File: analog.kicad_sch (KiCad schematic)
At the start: 7 parts, among them J15 Conn_02x12_Odd_Even, J16 Conn_01x06, J17 Conn_01x06, J18 Conn_01x06, J19 Conn_01x06, J20 Conn_01x06, J21 Conn_01x06

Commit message: Finished annotation
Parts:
- renumbered J16 to J1001, J17 to J1002, J18 to J1003, J15 to J1004, J19 to J1005, J20 to J1006, J21 to J1007
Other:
- sheet Analog Input 1 ports: added AIN1, AIN2; removed AOUT1, AOUT2
- sheet Analog Input 2 ports: added AIN1, AIN2; removed AOUT1, AOUT2
- sheet Analog Input 3 ports: added AIN1, AIN2; removed AOUT1, AOUT2
- sheet Analog Input 4 ports: added AIN1, AIN2; removed AOUT1, AOUT2
- sheet Analog Input 5 ports: added AIN1, AIN2; removed AOUT1, AOUT2
- sheet Analog Input 6 ports: added AIN1, AIN2; removed AOUT1, AOUT2
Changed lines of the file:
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@@
   (symbol (lib_id "power:+5V") (at 149.86 186.69 0) (unit 1)
     (in_bom yes) (on_board yes) (dnp no) (fields_autoplaced)
-    (property "Reference" "#PWR0189" (at 149.86 190.5 0)
+    (property "Reference" "#PWR01001" (at 149.86 190.5 0)
       (effects (font (size 1.27 1.27)) hide)
     )
@@
       (project "cad-enc-dec"
         (path "/894df1c3-1a5d-48b0-9966-84d5c2c2c705/27a43937-08d4-4f92-93fe-02e2fba5fc31"
-          (reference "#PWR0189") (unit 1)
+          (reference "#PWR01001") (unit 1)
         )
       )
@@
   (symbol (lib_id "Connector_Generic:Conn_01x06") (at 55.88 213.36 0) (unit 1)
     (in_bom yes) (on_board yes) (dnp no) (fields_autoplaced)
-    (property "Reference" "J19" (at 58.42 213.36 0)
+    (property "Reference" "J1005" (at 58.42 213.36 0)
       (effects (font (size 1.27 1.27)) (justify left))
     )
@@
       (project "cad-enc-dec"
         (path "/894df1c3-1a5d-48b0-9966-84d5c2c2c705/27a43937-08d4-4f92-93fe-02e2fba5fc31"
-          (reference "J19") (unit 1)
+          (reference "J1005") (unit 1)
         )
       )
@@
   (symbol (lib_id "power:+24V") (at 180.34 186.69 0) (unit 1)
     (in_bom yes) (on_board yes) (dnp no) (fields_autoplaced)
-    (property "Reference" "#PWR0190" (at 180.34 190.5 0)
+    (property "Reference" "#PWR01002" (at 180.34 190.5 0)
       (effects (font (size 1.27 1.27)) hide)
     )
@@
       (project "cad-enc-dec"
         (path "/894df1c3-1a5d-48b0-9966-84d5c2c2c705/27a43937-08d4-4f92-93fe-02e2fba5fc31"
-          (reference "#PWR0190") (unit 1)
+          (reference "#PWR01002") (unit 1)
         )
       )
@@
   (symbol (lib_id "Connector_Generic:Conn_01x06") (at 55.88 99.06 0) (unit 1)
     (in_bom yes) (on_board yes) (dnp no) (fields_autoplaced)
-    (property "Reference" "J16" (at 58.42 99.06 0)
+    (property "Reference" "J1001" (at 58.42 99.06 0)
       (effects (font (size 1.27 1.27)) (justify left))
     )
@@
       (project "cad-enc-dec"
         (path "/894df1c3-1a5d-48b0-9966-84d5c2c2c705/27a43937-08d4-4f92-93fe-02e2fba5fc31"
-          (reference "J16") (unit 1)
+          (reference "J1001") (unit 1)
         )
       )
@@
   (symbol (lib_id "power:GND") (at 180.34 214.63 0) (unit 1)
     (in_bom yes) (on_board yes) (dnp no) (fields_autoplaced)
-    (property "Reference" "#PWR0191" (at 180.34 220.98 0)
+    (property "Reference" "#PWR01004" (at 180.34 220.98 0)
       (effects (font (size 1.27 1.27)) hide)
     )
@@
       (project "cad-enc-dec"
         (path "/894df1c3-1a5d-48b0-9966-84d5c2c2c705/27a43937-08d4-4f92-93fe-02e2fba5fc31"
-          (reference "#PWR0191") (unit 1)
+          (reference "#PWR01004") (unit 1)
         )
       )
@@
   (symbol (lib_id "Connector_Generic:Conn_02x12_Odd_Even") (at 163.83 199.39 0) (unit 1)
     (in_bom yes) (on_board yes) (dnp no) (fields_autoplaced)
-    (property "Reference" "J15" (at 165.1 180.34 0)
+    (property "Reference" "J1004" (at 165.1 180.34 0)
       (effects (font (size 1.27 1.27)))
     )
@@
       (project "cad-enc-dec"
         (path "/894df1c3-1a5d-48b0-9966-84d5c2c2c705/27a43937-08d4-4f92-93fe-02e2fba5fc31"
-          (reference "J15") (unit 1)
+          (reference "J1004") (unit 1)
         )
       )
@@
   (symbol (lib_id "Connector_Generic:Conn_01x06") (at 55.88 251.46 0) (unit 1)
     (in_bom yes) (on_board yes) (dnp no) (fields_autoplaced)
-    (property "Reference" "J20" (at 58.42 251.46 0)
+    (property "Reference" "J1006" (at 58.42 251.46 0)
       (effects (font (size 1.27 1.27)) (justify left))
     )
@@
       (project "cad-enc-dec"
         (path "/894df1c3-1a5d-48b0-9966-84d5c2c2c705/27a43937-08d4-4f92-93fe-02e2fba5fc31"
-          (reference "J20") (unit 1)
+          (reference "J1006") (unit 1)
         )
       )
@@
   (symbol (lib_id "power:GND") (at 149.86 214.63 0) (unit 1)
     (in_bom yes) (on_board yes) (dnp no) (fields_autoplaced)
-    (property "Reference" "#PWR0192" (at 149.86 220.98 0)
+    (property "Reference" "#PWR01003" (at 149.86 220.98 0)
       (effects (font (size 1.27 1.27)) hide)
     )
@@
       (project "cad-enc-dec"
         (path "/894df1c3-1a5d-48b0-9966-84d5c2c2c705/27a43937-08d4-4f92-93fe-02e2fba5fc31"
-          (reference "#PWR0192") (unit 1)
+          (reference "#PWR01003") (unit 1)
         )
       )
@@
   (symbol (lib_id "Connector_Generic:Conn_01x06") (at 55.88 175.26 0) (unit 1)
     (in_bom yes) (on_board yes) (dnp no) (fields_autoplaced)
-    (property "Reference" "J18" (at 58.42 175.26 0)
+    (property "Reference" "J1003" (at 58.42 175.26 0)
       (effects (font (size 1.27 1.27)) (justify left))
     )
@@
       (project "cad-enc-dec"
         (path "/894df1c3-1a5d-48b0-9966-84d5c2c2c705/27a43937-08d4-4f92-93fe-02e2fba5fc31"
-          (reference "J18") (unit 1)
+          (reference "J1003") (unit 1)
         )
       )
@@
   (symbol (lib_id "Connector_Generic:Conn_01x06") (at 55.88 137.16 0) (unit 1)
     (in_bom yes) (on_board yes) (dnp no) (fields_autoplaced)
-    (property "Reference" "J17" (at 58.42 137.16 0)
+    (property "Reference" "J1002" (at 58.42 137.16 0)
       (effects (font (size 1.27 1.27)) (justify left))
     )
@@
       (project "cad-enc-dec"
         (path "/894df1c3-1a5d-48b0-9966-84d5c2c2c705/27a43937-08d4-4f92-93fe-02e2fba5fc31"
-          (reference "J17") (unit 1)
+          (reference "J1002") (unit 1)
         )
       )
@@
   (symbol (lib_id "Connector_Generic:Conn_01x06") (at 55.88 289.56 0) (unit 1)
     (in_bom yes) (on_board yes) (dnp no) (fields_autoplaced)
-    (property "Reference" "J21" (at 58.42 289.56 0)
+    (property "Reference" "J1007" (at 58.42 289.56 0)
       (effects (font (size 1.27 1.27)) (justify left))
     )
@@
       (project "cad-enc-dec"
         (path "/894df1c3-1a5d-48b0-9966-84d5c2c2c705/27a43937-08d4-4f92-93fe-02e2fba5fc31"
-          (reference "J21") (unit 1)
+          (reference "J1007") (unit 1)
         )
       )
@@
       (effects (font (size 1.27 1.27)) (justify left top))
     )
-    (pin "AOUT2" output (at 127 107.95 0)
-      (effects (font (size 2.54 2.54)) (justify right))
-    )
-    (pin "AOUT1" output (at 127 102.87 0)
+    (pin "AIN2" output (at 127 107.95 0)
+      (effects (font (size 2.54 2.54)) (justify right))
+    )
+    (pin "AIN1" output (at 127 102.87 0)
       (effects (font (size 2.54 2.54)) (justify right))
     )
@@
       (effects (font (size 1.27 1.27)) (justify left top))
     )
-    (pin "AOUT2" output (at 127 222.25 0)
-      (effects (font (size 2.54 2.54)) (justify right))
-    )
-    (pin "AOUT1" output (at 127 217.17 0)
+    (pin "AIN2" output (at 127 222.25 0)
+      (effects (font (size 2.54 2.54)) (justify right))
+    )
+    (pin "AIN1" output (at 127 217.17 0)
       (effects (font (size 2.54 2.54)) (justify right))
     )
@@
       (effects (font (size 1.27 1.27)) (justify left top))
     )
-    (pin "AOUT2" output (at 127 298.45 0)
-      (effects (font (size 2.54 2.54)) (justify right))
-    )
-    (pin "AOUT1" output (at 127 293.37 0)
+    (pin "AIN2" output (at 127 298.45 0)
+      (effects (font (size 2.54 2.54)) (justify right))
+    )
+    (pin "AIN1" output (at 127 293.37 0)
       (effects (font (size 2.54 2.54)) (justify right))
     )
@@
       (effects (font (size 1.27 1.27)) (justify left top))
     )
-    (pin "AOUT2" output (at 127 260.35 0)
-      (effects (font (size 2.54 2.54)) (justify right))
-    )
-    (pin "AOUT1" output (at 127 255.27 0)
+    (pin "AIN2" output (at 127 260.35 0)
+      (effects (font (size 2.54 2.54)) (justify right))
+    )
+    (pin "AIN1" output (at 127 255.27 0)
       (effects (font (size 2.54 2.54)) (justify right))
     )
@@
       (effects (font (size 1.27 1.27)) (justify left top))
     )
-    (pin "AOUT2" output (at 127 146.05 0)
-      (effects (font (size 2.54 2.54)) (justify right))
-    )
-    (pin "AOUT1" output (at 127 140.97 0)
+    (pin "AIN2" output (at 127 146.05 0)
+      (effects (font (size 2.54 2.54)) (justify right))
+    )
+    (pin "AIN1" output (at 127 140.97 0)
       (effects (font (size 2.54 2.54)) (justify right))
     )
@@
       (effects (font (size 1.27 1.27)) (justify left top))
     )
-    (pin "AOUT2" output (at 127 184.15 0)
-      (effects (font (size 2.54 2.54)) (justify right))
-    )
-    (pin "AOUT1" output (at 127 179.07 0)
-      (effects (font (size 2.54 2.54)) (justify right))
-    )
+    (pin "AIN2" output (at 127 184.15 0)
+      (effects (font (size 2.54 2.54)) (justify right))
+    )
+    (pin "AIN1" output (at 127 179.07 0)
+      (effects (font (size 2.54 2.54)) (justify right))
+    )

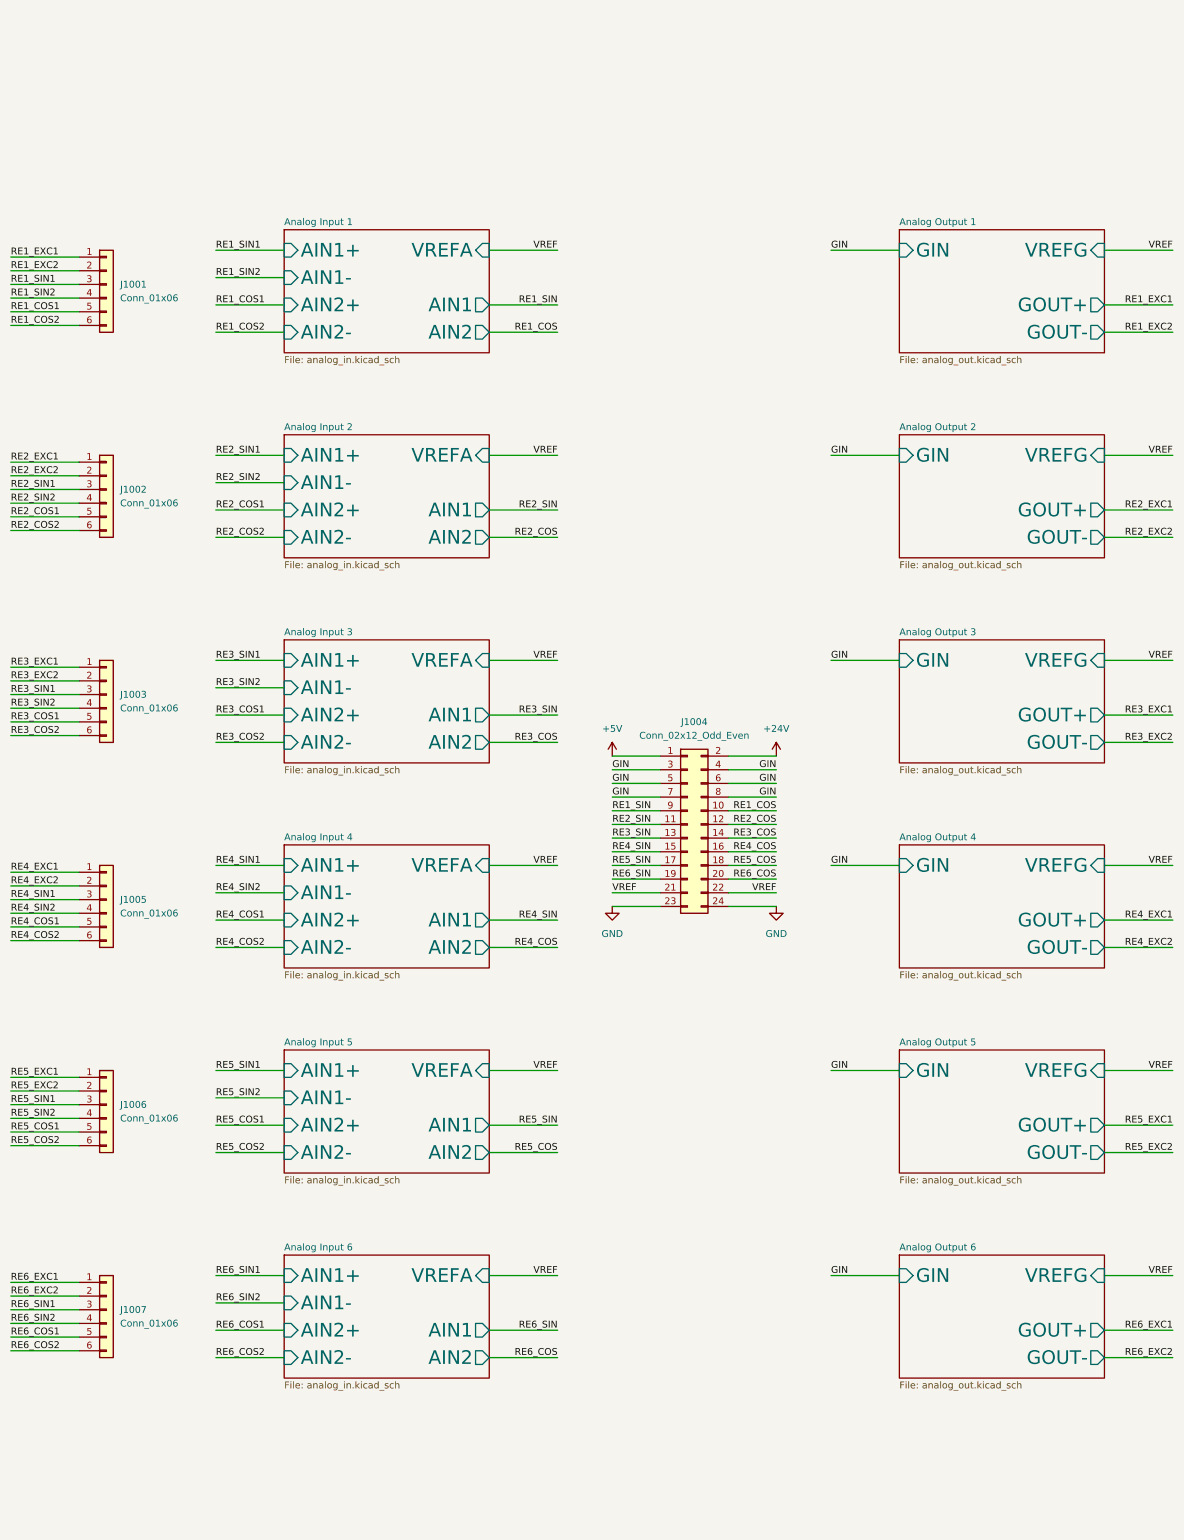
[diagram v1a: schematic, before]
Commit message: Merged receiver and transmitter
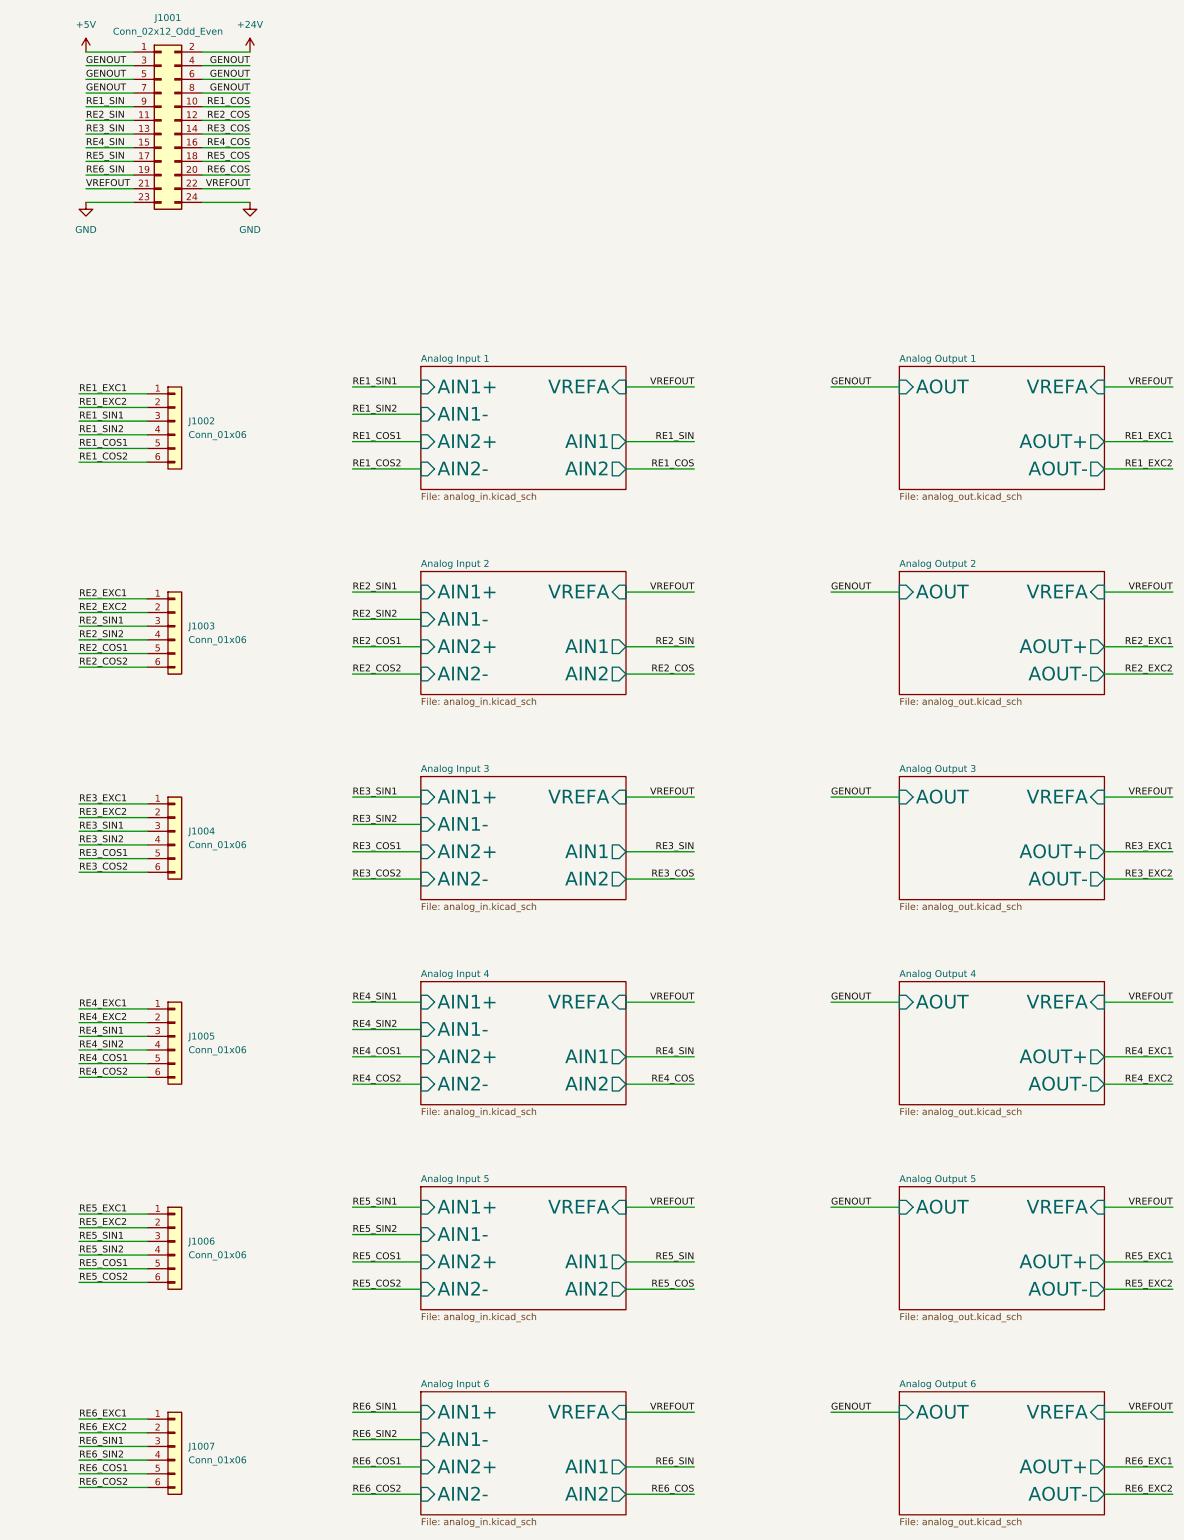
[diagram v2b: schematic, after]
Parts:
- renumbered J1004 to J1001, J1001 to J1002, J1002 to J1003, J1003 to J1004
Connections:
- net GIN renamed GENOUT
- net VREF renamed VREFOUT
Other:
- sheet Analog Output 1 ports: added AOUT, AOUT+, AOUT-, VREFA; removed GIN, GOUT+, GOUT-, VREFG
- sheet Analog Output 2 ports: added AOUT, AOUT+, AOUT-, VREFA; removed GIN, GOUT+, GOUT-, VREFG
- sheet Analog Output 3 ports: added AOUT, AOUT+, AOUT-, VREFA; removed GIN, GOUT+, GOUT-, VREFG
- sheet Analog Output 4 ports: added AOUT, AOUT+, AOUT-, VREFA; removed GIN, GOUT+, GOUT-, VREFG
- sheet Analog Output 5 ports: added AOUT, AOUT+, AOUT-, VREFA; removed GIN, GOUT+, GOUT-, VREFG
- sheet Analog Output 6 ports: added AOUT, AOUT+, AOUT-, VREFA; removed GIN, GOUT+, GOUT-, VREFG
- moved on the sheet: J1001, J1002, J1003, J1004, J1005, J1006, J1007
